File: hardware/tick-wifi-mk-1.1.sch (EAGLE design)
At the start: 25 parts, among them IC1 MAX7219, IC2 MAX7219, IC3 74HC125, IC4 LD1117 5V

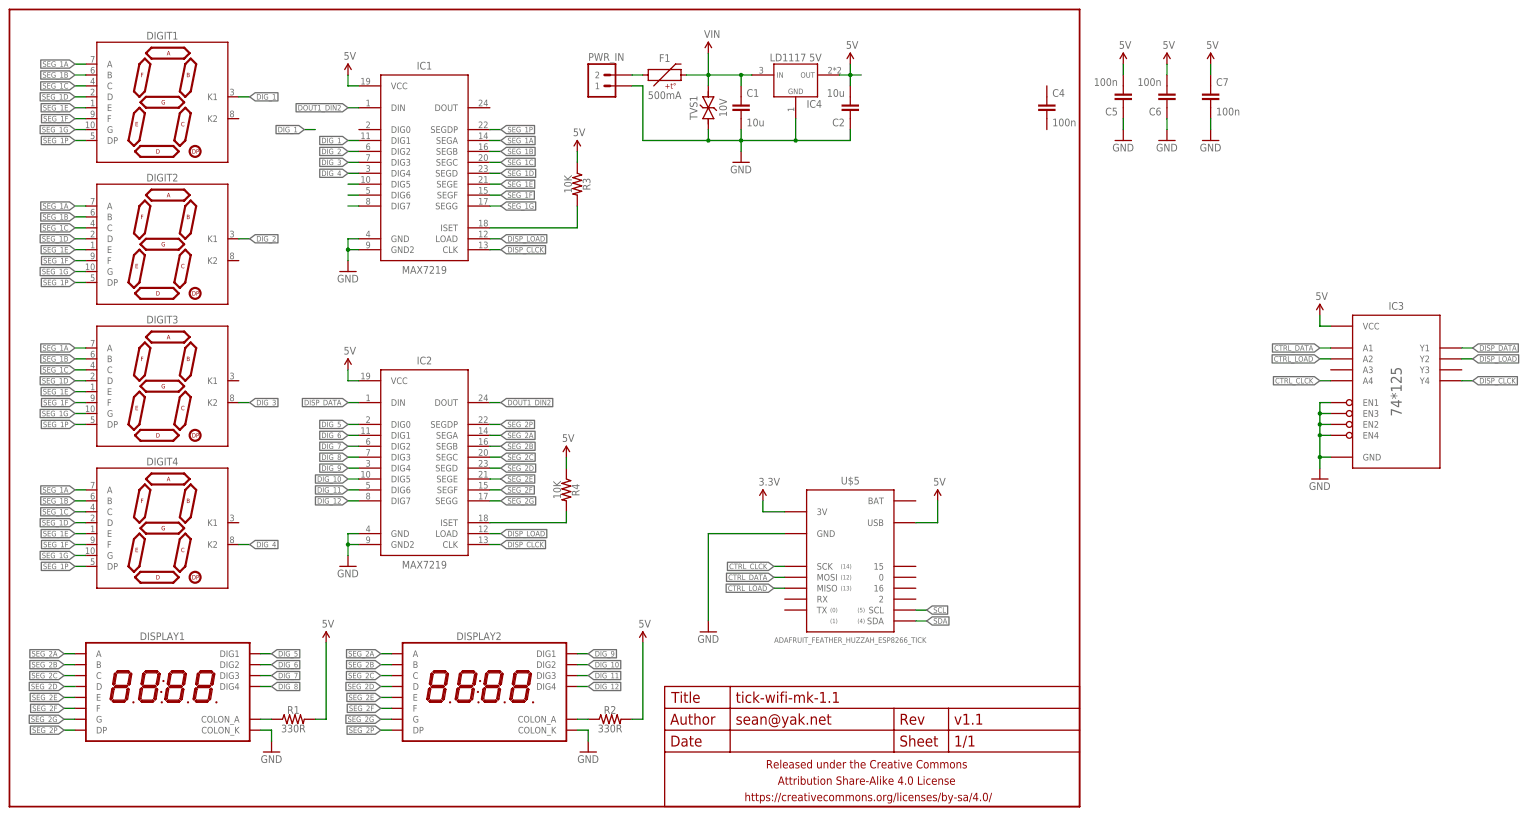
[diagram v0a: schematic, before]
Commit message: layout finished for wifail board
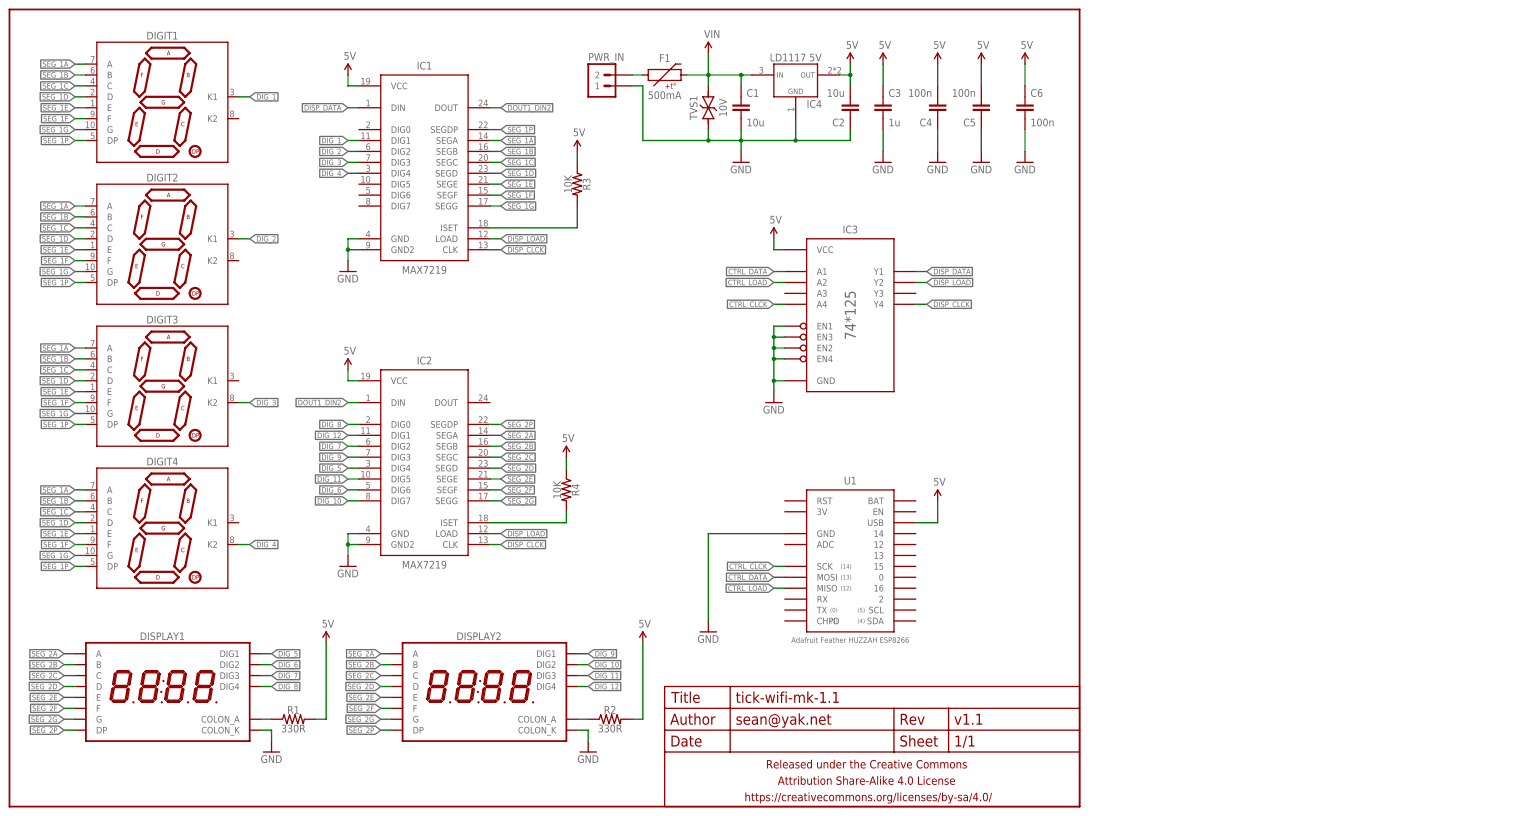
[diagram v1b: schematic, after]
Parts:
- removed C7: 100n, a_parts:CAPACITOR-CERAMICC0603
- removed U$5: ADAFRUIT_FEATHER_HUZZAH_ESP8266_TICK, a_parts:ADAFRUIT_FEATHER_HUZZAH_ESP8266_TICK
- added C3: 1u, a_parts:CAPACITOR-CERAMICC0805
- added U1: Adafruit Feather HUZZAH ESP8266, a_parts:ADAFRUIT_FEATHER_HUZZAH_ESP8266
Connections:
- removed net 3.3V: U$5.3V
- removed net N$7: IC1.DIG5
- removed net N$8: IC1.DIG6
- removed net N$9: IC1.DIG7
- removed net SCL: U$5.SCL
- removed net SDA: U$5.SDA
- net 5V: now also C3.1, C4.2, C6.1, U1.USB; no longer C6.2, C7.1, U$5.USB
- net CTRL_CLCK: now also U1.SCK; no longer U$5.SCK
- net CTRL_DATA: now also U1.MOSI; no longer U$5.MOSI
- net CTRL_LOAD: now also U1.MISO; no longer U$5.MISO
- net DIG_10: now also IC2.DIG7; no longer IC2.DIG5
- net DIG_11: now also IC2.DIG5; no longer IC2.DIG6
- net DIG_12: now also IC2.DIG1; no longer IC2.DIG7
- net DIG_5: now also IC2.DIG4; no longer IC2.DIG0
- net DIG_6: now also IC2.DIG6; no longer IC2.DIG1
- net DIG_8: now also IC2.DIG0; no longer IC2.DIG3
- net DIG_9: now also IC2.DIG3; no longer IC2.DIG4
- net DISP_DATA: now also IC1.DIN; no longer IC2.DIN
- net DOUT1_DIN2: now also IC1.DOUT, IC2.DIN; no longer IC1.DIN, IC2.DOUT
- net GND: now also C3.2, C4.1, C6.2, U1.GND; no longer C6.1, C7.2, U$5.GND
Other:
- moved on the sheet: C4, C5, C6, IC3

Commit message: more wip
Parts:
- removed C3: 1u, a_parts:CAPACITOR-CERAMICC0805
- removed C4: 100n, a_parts:CAPACITOR-CERAMICC0603
- removed PWR_IN: M02PTH-CENTERED-R+, A_butts:M02PTH-CENTERED-R+
- added C7: 100n, a_parts:CAPACITOR-CERAMICC0603
- added PWR1: DCBARRELPTH, a_parts:DCBARRELPTH
- DIGIT1, DIGIT2, DIGIT3, DIGIT4: device A_butts:7SEG_1DIGPTH-25.4MM-BARE -> a_parts:7SEG_1DIGPTH-25.4MM-BARE
- DISPLAY1, DISPLAY2: value 7SEG_4DIGIT_COLON14.2MM-CC -> 7SEG_4DIGIT_COLON_APOS; device a_parts:7SEG_4DIGIT_COLON14.2MM-CC -> a_parts:7SEG_4DIGIT_COLON_APOS
- F1: device A_butts:PTCPTC-1210 -> a_parts:PTCPTC-1210
- FRAME1: device A_butts:FRAME-LETTERNO_PACKAGE -> a_parts:FRAME-LETTERNO_PACKAGE
- TVS1: device A_butts:TVSSMA -> a_parts:TVSSMA
- U1: value Adafruit Feather HUZZAH ESP8266 -> ADAFRUIT_FEATHER_HUZZAH_ESP8266_TICK; device a_parts:ADAFRUIT_FEATHER_HUZZAH_ESP8266 -> a_parts:ADAFRUIT_FEATHER_HUZZAH_ESP8266_TICK
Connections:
- net 5V: now also C6.2, C7.1; no longer C3.1, C4.2, C6.1
- net DIG_10: now also IC2.DIG5; no longer IC2.DIG7
- net DIG_11: now also IC2.DIG6; no longer IC2.DIG5
- net DIG_12: now also IC2.DIG7; no longer IC2.DIG1
- net DIG_5: now also IC2.DIG0; no longer IC2.DIG4
- net DIG_6: now also IC2.DIG1; no longer IC2.DIG6
- net DIG_8: now also IC2.DIG3; no longer IC2.DIG0
- net DIG_9: now also IC2.DIG4; no longer IC2.DIG3
- net GND: now also C6.1, C7.2, DISPLAY1.CL_K, DISPLAY2.CL_K, PWR1.BRK; no longer C3.2, C4.1, C6.2, DISPLAY1.COLON_K, DISPLAY2.COLON_K, PWR_IN.1
- net N$1: now also PWR1.PWR; no longer PWR_IN.2
- net N$3: now also DISPLAY1.CL_A; no longer DISPLAY1.COLON_A
- net N$5: now also DISPLAY2.CL_A; no longer DISPLAY2.COLON_A
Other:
- moved on the sheet: C1, C2, C5, C6, F1, IC1, IC2, IC3, IC4, R1, R2, R3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

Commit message: more wip again
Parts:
- removed U1: ADAFRUIT_FEATHER_HUZZAH_ESP8266_TICK, a_parts:ADAFRUIT_FEATHER_HUZZAH_ESP8266_TICK
- added JP1: M05PTH-CENTERED, a_parts:M05PTH-CENTERED
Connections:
- net 5V: now also JP1.5; no longer U1.USB
- net CTRL_CLCK: now also JP1.3; no longer U1.SCK
- net CTRL_DATA: now also JP1.2; no longer U1.MOSI
- net CTRL_LOAD: now also JP1.1; no longer U1.MISO
- net DIG_2: now also IC1.DIG3; no longer IC1.DIG2
- net DIG_3: now also IC1.DIG2; no longer IC1.DIG3
- net DIG_4: now also IC1.DIG0; no longer IC1.DIG4
- net GND: now also JP1.4; no longer U1.GND
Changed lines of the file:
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@@
 <part name="DISPLAY1" library="a_parts" deviceset="7SEG_4DIGIT_COLON_APOS" device=""/>
 <part name="DISPLAY2" library="a_parts" deviceset="7SEG_4DIGIT_COLON_APOS" device=""/>
-<part name="U1" library="a_parts" deviceset="ADAFRUIT_FEATHER_HUZZAH_ESP8266_TICK" device=""/>
+<part name="PWR1" library="a_parts" deviceset="DCBARREL" device="PTH"/>
+<part name="JP1" library="a_parts" deviceset="M05" device="PTH-CENTERED"/>
 <part name="SUPPLY3" library="a_parts" deviceset="5V" device=""/>
 <part name="GND10" library="a_parts" deviceset="GND" device=""/>
-<part name="PWR1" library="a_parts" deviceset="DCBARREL" device="PTH"/>
 </parts>
 <sheets>
@@
 <instance part="DISPLAY1" gate="G$1" x="101.6" y="109.22"/>
 <instance part="DISPLAY2" gate="G$1" x="187.96" y="109.22"/>
-<instance part="U1" gate="G$1" x="101.6" y="68.58"/>
-<instance part="SUPPLY3" gate="G$1" x="116.84" y="83.82"/>
-<instance part="GND10" gate="1" x="68.58" y="68.58"/>
 <instance part="PWR1" gate="G$1" x="20.32" y="30.48"/>
+<instance part="JP1" gate="G$1" x="96.52" y="73.66"/>
+<instance part="SUPPLY3" gate="G$1" x="121.92" y="81.28" rot="MR0"/>
+<instance part="GND10" gate="1" x="121.92" y="63.5" rot="MR0"/>
 </instances>
 <busses>
@@
 <segment>
 <pinref part="GND10" gate="1" pin="GND"/>
-<wire x1="68.58" y1="71.12" x2="68.58" y2="73.66" width="0.1524" layer="91"/>
-<pinref part="U1" gate="G$1" pin="GND"/>
-<wire x1="68.58" y1="73.66" x2="88.9" y2="73.66" width="0.1524" layer="91"/>
+<wire x1="121.92" y1="66.04" x2="121.92" y2="76.2" width="0.1524" layer="91"/>
+<wire x1="121.92" y1="76.2" x2="104.14" y2="76.2" width="0.1524" layer="91"/>
+<pinref part="JP1" gate="G$1" pin="4"/>
 </segment>
 </net>
@@
 </segment>
 <segment>
+<wire x1="83.82" y1="157.48" x2="86.36" y2="157.48" width="0.1524" layer="91"/>
+<label x="83.82" y="157.48" size="1.27" layer="95" rot="MR0" xref="yes"/>
+<pinref part="IC1" gate="G$1" pin="DIG3"/>
+</segment>
+</net>
+<net name="DIG_4" class="0">
+<segment>
+<wire x1="55.88" y1="60.96" x2="53.34" y2="60.96" width="0.1524" layer="91"/>
+<label x="55.88" y="60.96" size="1.27" layer="95" xref="yes"/>
+<pinref part="DIGIT4" gate="G$1" pin="K2"/>
+</segment>
+<segment>
+<wire x1="83.82" y1="165.1" x2="86.36" y2="165.1" width="0.1524" layer="91"/>
+<label x="83.82" y="165.1" size="1.27" layer="95" rot="MR0" xref="yes"/>
+<pinref part="IC1" gate="G$1" pin="DIG0"/>
+</segment>
+</net>
+<net name="DIG_3" class="0">
+<segment>
+<wire x1="55.88" y1="93.98" x2="53.34" y2="93.98" width="0.1524" layer="91"/>
+<label x="55.88" y="93.98" size="1.27" layer="95" xref="yes"/>
+<pinref part="DIGIT3" gate="G$1" pin="K2"/>
+</segment>
+<segment>
 <wire x1="83.82" y1="160.02" x2="86.36" y2="160.02" width="0.1524" layer="91"/>
 <label x="83.82" y="160.02" size="1.27" layer="95" rot="MR0" xref="yes"/>
 <pinref part="IC1" gate="G$1" pin="DIG2"/>
-</segment>
-</net>
-<net name="DIG_4" class="0">
-<segment>
-<wire x1="55.88" y1="60.96" x2="53.34" y2="60.96" width="0.1524" layer="91"/>
-<label x="55.88" y="60.96" size="1.27" layer="95" xref="yes"/>
-<pinref part="DIGIT4" gate="G$1" pin="K2"/>
-</segment>
-<segment>
-<wire x1="83.82" y1="154.94" x2="86.36" y2="154.94" width="0.1524" layer="91"/>
-<label x="83.82" y="154.94" size="1.27" layer="95" rot="MR0" xref="yes"/>
-<pinref part="IC1" gate="G$1" pin="DIG4"/>
-</segment>
-</net>
-<net name="DIG_3" class="0">
-<segment>
-<wire x1="55.88" y1="93.98" x2="53.34" y2="93.98" width="0.1524" layer="91"/>
-<label x="55.88" y="93.98" size="1.27" layer="95" xref="yes"/>
-<pinref part="DIGIT3" gate="G$1" pin="K2"/>
-</segment>
-<segment>
-<wire x1="83.82" y1="157.48" x2="86.36" y2="157.48" width="0.1524" layer="91"/>
-<label x="83.82" y="157.48" size="1.27" layer="95" rot="MR0" xref="yes"/>
-<pinref part="IC1" gate="G$1" pin="DIG3"/>
 </segment>
 </net>
@@
 </segment>
 <segment>
-<pinref part="U1" gate="G$1" pin="USB"/>
-<wire x1="114.3" y1="76.2" x2="116.84" y2="76.2" width="0.1524" layer="91"/>
 <pinref part="SUPPLY3" gate="G$1" pin="5V"/>
-<wire x1="116.84" y1="76.2" x2="116.84" y2="83.82" width="0.1524" layer="91"/>
+<wire x1="121.92" y1="81.28" x2="121.92" y2="78.74" width="0.1524" layer="91"/>
+<wire x1="121.92" y1="78.74" x2="104.14" y2="78.74" width="0.1524" layer="91"/>
+<pinref part="JP1" gate="G$1" pin="5"/>
 </segment>
 </net>
@@
 </segment>
 <segment>
-<label x="86.36" y="63.5" size="1.27" layer="95" rot="R180" xref="yes"/>
-<wire x1="86.36" y1="63.5" x2="88.9" y2="63.5" width="0.1524" layer="91"/>
-<pinref part="U1" gate="G$1" pin="MOSI"/>
+<label x="106.68" y="71.12" size="1.27" layer="95" rot="MR180" xref="yes"/>
+<wire x1="106.68" y1="71.12" x2="104.14" y2="71.12" width="0.1524" layer="91"/>
+<pinref part="JP1" gate="G$1" pin="2"/>
 </segment>
 </net>
@@
 </segment>
 <segment>
-<wire x1="86.36" y1="60.96" x2="88.9" y2="60.96" width="0.1524" layer="91"/>
-<label x="86.36" y="60.96" size="1.27" layer="95" rot="R180" xref="yes"/>
-<pinref part="U1" gate="G$1" pin="MISO"/>
+<wire x1="106.68" y1="68.58" x2="104.14" y2="68.58" width="0.1524" layer="91"/>
+<label x="106.68" y="68.58" size="1.27" layer="95" rot="MR180" xref="yes"/>
+<pinref part="JP1" gate="G$1" pin="1"/>
 </segment>
 </net>
@@
 </segment>
 <segment>
-<wire x1="86.36" y1="66.04" x2="88.9" y2="66.04" width="0.1524" layer="91"/>
-<label x="86.36" y="66.04" size="1.27" layer="95" rot="R180" xref="yes"/>
-<pinref part="U1" gate="G$1" pin="SCK"/>
-</segment>
-</net>
+<wire x1="106.68" y1="73.66" x2="104.14" y2="73.66" width="0.1524" layer="91"/>
+<label x="106.68" y="73.66" size="1.27" layer="95" rot="MR180" xref="yes"/>
+<pinref part="JP1" gate="G$1" pin="3"/>
+</segment>
+</net>

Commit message: wip
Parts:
- R1, R2: device a_parts:RESISTORR0805 -> a_parts:RESISTORR0603
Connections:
- net DIG_1: now also IC1.DIG0; no longer IC1.DIG1
- net DIG_2: now also IC1.DIG1; no longer IC1.DIG3
- net DIG_4: now also IC1.DIG3; no longer IC1.DIG0

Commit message: new tick version
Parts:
- removed PWR1: DCBARRELPTH, a_parts:DCBARRELPTH
- added JP2: M02PTH-CENTERED-R+, a_parts:M02PTH-CENTERED-R+
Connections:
- net GND: now also JP2.1; no longer PWR1.BRK
- net N$1: now also JP2.2; no longer PWR1.PWR
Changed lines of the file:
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@@
 <grid distance="100" unitdist="mil" unit="mil" style="lines" multiple="1" display="yes" altdistance="2" altunitdist="mil" altunit="mil"/>
 <layers>
-<layer number="1" name="Top" color="4" fill="1" visible="yes" active="no"/>
-<layer number="16" name="Bottom" color="1" fill="1" visible="yes" active="no"/>
-<layer number="17" name="Pads" color="2" fill="1" visible="yes" active="no"/>
-<layer number="18" name="Vias" color="2" fill="1" visible="yes" active="no"/>
-<layer number="19" name="Unrouted" color="6" fill="1" visible="yes" active="no"/>
-<layer number="20" name="Dimension" color="15" fill="1" visible="yes" active="no"/>
-<layer number="21" name="tPlace" color="7" fill="1" visible="yes" active="no"/>
-<layer number="22" name="bPlace" color="7" fill="1" visible="yes" active="no"/>
-<layer number="23" name="tOrigins" color="15" fill="1" visible="yes" active="no"/>
-<layer number="24" name="bOrigins" color="15" fill="1" visible="yes" active="no"/>
-<layer number="25" name="tNames" color="7" fill="1" visible="yes" active="no"/>
-<layer number="26" name="bNames" color="7" fill="1" visible="yes" active="no"/>
-<layer number="27" name="tValues" color="7" fill="1" visible="yes" active="no"/>
-<layer number="28" name="bValues" color="7" fill="1" visible="yes" active="no"/>
+<layer number="1" name="Top" color="4" fill="1" visible="no" active="no"/>
+<layer number="16" name="Bottom" color="1" fill="1" visible="no" active="no"/>
+<layer number="17" name="Pads" color="2" fill="1" visible="no" active="no"/>
+<layer number="18" name="Vias" color="2" fill="1" visible="no" active="no"/>
+<layer number="19" name="Unrouted" color="6" fill="1" visible="no" active="no"/>
+<layer number="20" name="Dimension" color="15" fill="1" visible="no" active="no"/>
+<layer number="21" name="tPlace" color="7" fill="1" visible="no" active="no"/>
+<layer number="22" name="bPlace" color="7" fill="1" visible="no" active="no"/>
+<layer number="23" name="tOrigins" color="15" fill="1" visible="no" active="no"/>
+<layer number="24" name="bOrigins" color="15" fill="1" visible="no" active="no"/>
+<layer number="25" name="tNames" color="7" fill="1" visible="no" active="no"/>
+<layer number="26" name="bNames" color="7" fill="1" visible="no" active="no"/>
+<layer number="27" name="tValues" color="7" fill="1" visible="no" active="no"/>
+<layer number="28" name="bValues" color="7" fill="1" visible="no" active="no"/>
 <layer number="29" name="tStop" color="7" fill="3" visible="no" active="no"/>
 <layer number="30" name="bStop" color="7" fill="6" visible="no" active="no"/>
@@
 <layer number="35" name="tGlue" color="7" fill="4" visible="no" active="no"/>
 <layer number="36" name="bGlue" color="7" fill="5" visible="no" active="no"/>
-<layer number="37" name="tTest" color="7" fill="1" visible="yes" active="no"/>
-<layer number="38" name="bTest" color="7" fill="1" visible="yes" active="no"/>
+<layer number="37" name="tTest" color="7" fill="1" visible="no" active="no"/>
+<layer number="38" name="bTest" color="7" fill="1" visible="no" active="no"/>
 <layer number="39" name="tKeepout" color="4" fill="11" visible="no" active="no"/>
 <layer number="40" name="bKeepout" color="1" fill="11" visible="no" active="no"/>
@@
 <layer number="44" name="Drills" color="7" fill="1" visible="no" active="no"/>
 <layer number="45" name="Holes" color="7" fill="1" visible="no" active="no"/>
-<layer number="46" name="Milling" color="3" fill="1" visible="yes" active="no"/>
-<layer number="47" name="Measures" color="7" fill="1" visible="yes" active="no"/>
-<layer number="48" name="Document" color="7" fill="1" visible="yes" active="no"/>
-<layer number="49" name="Reference" color="7" fill="1" visible="yes" active="no"/>
-<layer number="50" name="dxf" color="7" fill="1" visible="yes" active="no"/>
-<layer number="51" name="tDocu" color="6" fill="1" visible="yes" active="no"/>
-<layer number="52" name="bDocu" color="6" fill="1" visible="yes" active="no"/>
-<layer number="53" name="tGND_GNDA" color="7" fill="9" visible="yes" active="no"/>
-<layer number="54" name="bGND_GNDA" color="1" fill="9" visible="yes" active="no"/>
-<layer number="56" name="wert" color="7" fill="1" visible="yes" active="no"/>
-<layer number="57" name="tCAD" color="7" fill="1" visible="yes" active="no"/>
-<layer number="59" name="tCarbon" color="7" fill="1" visible="yes" active="no"/>
-<layer number="60" name="bCarbon" color="7" fill="1" visible="yes" active="no"/>
+<layer number="46" name="Milling" color="3" fill="1" visible="no" active="no"/>
+<layer number="47" name="Measures" color="7" fill="1" visible="no" active="no"/>
+<layer number="48" name="Document" color="7" fill="1" visible="no" active="no"/>
+<layer number="49" name="Reference" color="7" fill="1" visible="no" active="no"/>
+<layer number="50" name="dxf" color="7" fill="1" visible="no" active="no"/>
+<layer number="51" name="tDocu" color="6" fill="1" visible="no" active="no"/>
+<layer number="52" name="bDocu" color="6" fill="1" visible="no" active="no"/>
+<layer number="53" name="tGND_GNDA" color="7" fill="9" visible="no" active="no"/>
+<layer number="54" name="bGND_GNDA" color="1" fill="9" visible="no" active="no"/>
+<layer number="56" name="wert" color="7" fill="1" visible="no" active="no"/>
+<layer number="57" name="tCAD" color="7" fill="1" visible="no" active="no"/>
+<layer number="59" name="tCarbon" color="7" fill="1" visible="no" active="no"/>
+<layer number="60" name="bCarbon" color="7" fill="1" visible="no" active="no"/>
 <layer number="90" name="Modules" color="5" fill="1" visible="yes" active="yes"/>
 <layer number="91" name="Nets" color="2" fill="1" visible="yes" active="yes"/>
@@
 <part name="DISPLAY1" library="a_parts" deviceset="7SEG_4DIGIT_COLON_APOS" device=""/>
 <part name="DISPLAY2" library="a_parts" deviceset="7SEG_4DIGIT_COLON_APOS" device=""/>
-<part name="PWR1" library="a_parts" deviceset="DCBARREL" device="PTH"/>
 <part name="JP1" library="a_parts" deviceset="M05" device="PTH-CENTERED"/>
 <part name="SUPPLY3" library="a_parts" deviceset="5V" device=""/>
 <part name="GND10" library="a_parts" deviceset="GND" device=""/>
+<part name="JP2" library="a_parts" deviceset="M02" device="PTH-CENTERED-R+"/>
 </parts>
 <sheets>
@@
 <instance part="DISPLAY1" gate="G$1" x="101.6" y="109.22"/>
 <instance part="DISPLAY2" gate="G$1" x="187.96" y="109.22"/>
-<instance part="PWR1" gate="G$1" x="20.32" y="30.48"/>
 <instance part="JP1" gate="G$1" x="96.52" y="73.66"/>
 <instance part="SUPPLY3" gate="G$1" x="121.92" y="81.28" rot="MR0"/>
 <instance part="GND10" gate="1" x="121.92" y="63.5" rot="MR0"/>
+<instance part="JP2" gate="G$1" x="12.7" y="27.94"/>
 </instances>
 <busses>
@@
 <pinref part="C2" gate="G$1" pin="1"/>
 <pinref part="C1" gate="G$1" pin="2"/>
-<pinref part="PWR1" gate="G$1" pin="BRK"/>
+<pinref part="JP2" gate="G$1" pin="1"/>
 </segment>
 <segment>
@@
 <pinref part="F1" gate="G$1" pin="1"/>
 <wire x1="22.86" y1="33.02" x2="30.48" y2="33.02" width="0.1524" layer="91"/>
-<pinref part="PWR1" gate="G$1" pin="PWR"/>
-</segment>
-</net>
+<pinref part="JP2" gate="G$1" pin="2"/>
+</segment>
+</net>
